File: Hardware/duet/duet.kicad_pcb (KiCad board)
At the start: 2 copper layers, 52 parts, among them CN1 A71-05H5-111N1, U1 LFE5U-45F-6BG256C, U2 W956D8MBYA5I, U3 W25Q128JVSIQTR, U4 SII9022ACNU, U5 RT9013-12GB, U6 TPS563201DDCR, U7 RCLAMP0514M, U8 RCLAMP0514M, U9 ESP32-S3-WROOM-1, X1 OT322525MJBA4SL

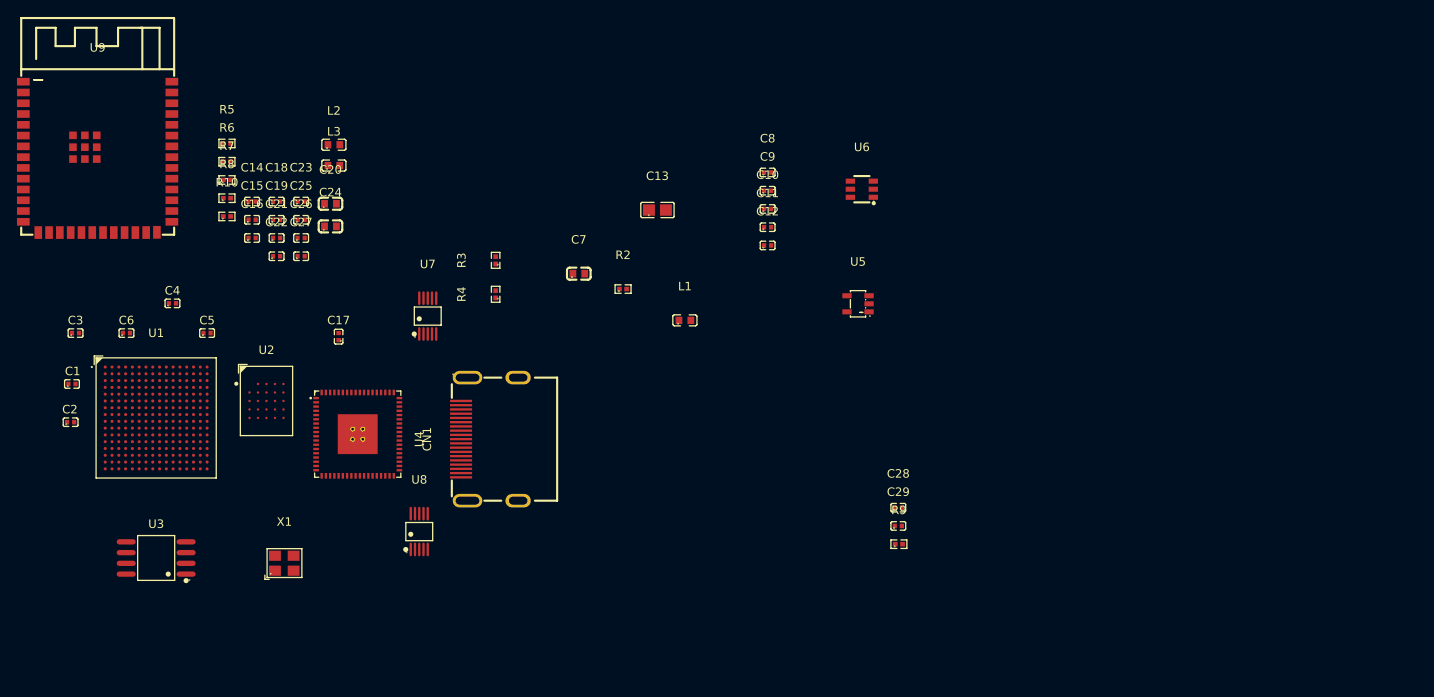
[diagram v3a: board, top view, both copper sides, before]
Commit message: Add mezzanine connector and finalze HDMI
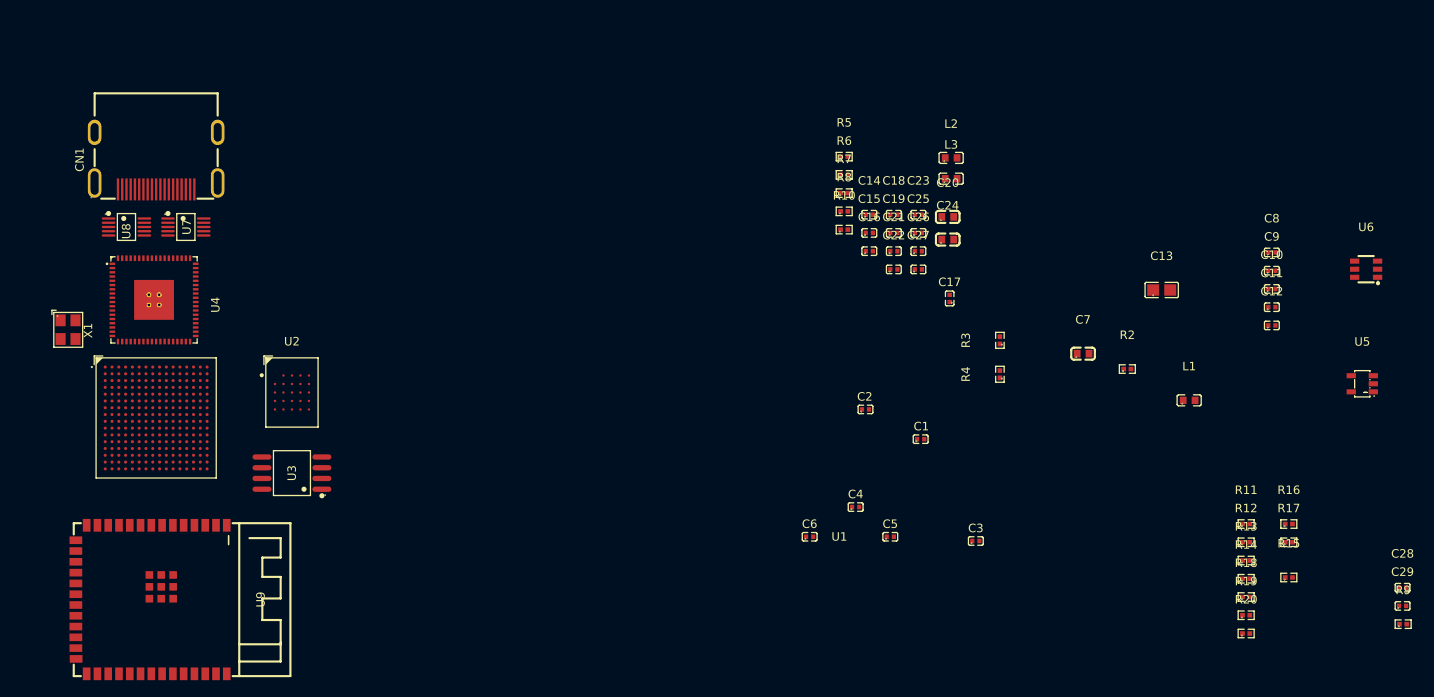
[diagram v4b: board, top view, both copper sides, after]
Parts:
- added R11: 4.7k, easyeda2kicad:R0402, F.Cu at (239.4, 93.0)
- added R12: 4.7k, easyeda2kicad:R0402, F.Cu at (239.4, 95.2)
- added R13: 4.7k, easyeda2kicad:R0402, F.Cu at (239.4, 97.3)
- added R14: 4.7k, easyeda2kicad:R0402, F.Cu at (239.4, 99.5)
- added R15: 10k, easyeda2kicad:R0402, F.Cu at (244.5, 99.3)
- added R16: 10k, easyeda2kicad:R0402, F.Cu at (244.5, 93.0)
- added R17: 10k, easyeda2kicad:R0402, F.Cu at (244.5, 95.2)
- added R18: 4.7k, easyeda2kicad:R0402, F.Cu at (239.4, 101.6)
- added R19: 4.7k, easyeda2kicad:R0402, F.Cu at (239.4, 103.8)
- added R20: 4.7k, easyeda2kicad:R0402, F.Cu at (239.4, 105.9)
- moved C3 108.9 mm to (207.6, 95.0)
- moved C1 100.2 mm to (201.1, 83.0)
- moved C2 93.7 mm to (194.6, 79.5)
- moved C5 84.0 mm to (197.5, 94.5)
- moved C6 84.0 mm to (188.0, 94.5)
- moved C4 84.0 mm to (193.4, 91.0)
- moved C20 72.7 mm to (204.3, 56.8)
- moved C24 72.7 mm to (204.3, 59.5)
- moved C14 72.7 mm to (195.0, 56.5)
- moved C15 72.7 mm to (195.0, 58.7)
- moved C16 72.7 mm to (195.0, 60.9)
- moved C18 72.7 mm to (197.9, 56.5)
- moved C19 72.7 mm to (197.9, 58.7)
- moved C21 72.7 mm to (197.9, 60.9)
- moved C22 72.7 mm to (197.9, 63.0)
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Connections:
- U1 pad A10: unconnected-(U1A-PT51B-PadA10) -> D9
- U1 pad A11: unconnected-(U1A-PT71A-PadA11) -> D16
- U1 pad A12: unconnected-(U1A-PT71B-PadA12) -> D18
- U1 pad A8: unconnected-(U1A-PT38B/PCLKC0_0-PadA8) -> /FPGA/FPGA-PCLK
- U1 pad A9: unconnected-(U1A-PT51A-PadA9) -> D7
- U1 pad B10: unconnected-(U1A-PT53A-PadB10) -> D8
- U1 pad B11: unconnected-(U1A-PT58A-PadB11) -> D12
- U1 pad B12: unconnected-(U1A-PT74A-PadB12) -> D19
- U1 pad B13: unconnected-(U1A-PT78A-PadB13) -> D23
- U1 pad B8: /FPGA/FPGA-PCLK -> D2
- U1 pad B9: unconnected-(U1A-PT47A/GR_PCLK1_0-PadB9) -> D3
- U1 pad C10: unconnected-(U1A-PT53B-PadC10) -> D10
- U1 pad C11: unconnected-(U1A-PT58B-PadC11) -> D14
- U1 pad C12: unconnected-(U1A-PT74B-PadC12) -> D21
- U1 pad C8: unconnected-(U1A-PT44A/PCLKT1_0-PadC8) -> D0
- U1 pad C9: unconnected-(U1A-PT47B/GR_PCLK1_1-PadC9) -> D5
- U1 pad D10: unconnected-(U1A-PT56A-PadD10) -> D11
- U1 pad D11: unconnected-(U1A-PT69A-PadD11) -> D15
- U1 pad D12: unconnected-(U1A-PT76A-PadD12) -> D20
- U1 pad D8: unconnected-(U1A-PT42B/PCLKC1_1-PadD8) -> D1
- U1 pad D9: unconnected-(U1A-PT49A-PadD9) -> D4
- U1 pad E10: unconnected-(U1A-PT56B-PadE10) -> D13
- U1 pad E11: unconnected-(U1A-PT69B-PadE11) -> D17
- U1 pad E12: unconnected-(U1A-PT76B-PadE12) -> D22
- U1 pad E8: unconnected-(U1A-PT42A/PCLKT1_1-PadE8) -> IDCK
- U1 pad E9: unconnected-(U1A-PT49B-PadE9) -> D6
- U1 pad N10: unconnected-(U1B-CFG_0-PadN10) -> GND
- U1 pad P10: unconnected-(U1B-CFG_1-PadP10) -> Net-(U1B-CFG_1)
- U1 pad R10: unconnected-(U1B-CFG_2-PadR10) -> GND
- U9 pad 10: unconnected-(U9-IO17-Pad10) -> FPGA-PROGRAMN
- U9 pad 4: unconnected-(U9-IO4-Pad4) -> FPGA-TCK
- U9 pad 5: unconnected-(U9-IO5-Pad5) -> FPGA-TDI
- U9 pad 6: unconnected-(U9-IO6-Pad6) -> FPGA-TMS
- U9 pad 7: unconnected-(U9-IO7-Pad7) -> FPGA-TDO
- U9 pad 8: unconnected-(U9-IO15-Pad8) -> FPGA-DONE
- U9 pad 9: unconnected-(U9-IO16-Pad9) -> FPGA-INITN
